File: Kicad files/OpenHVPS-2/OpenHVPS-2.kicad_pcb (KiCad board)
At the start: 2 copper layers, 47.1 x 20.5 mm, 67 parts, among them J1 Conn_01x03_Male, J2 Conn_01x03_Male, Q1 FQT7N10, Q2 BC846, Q3 MMDT3906, U1 74HC14, U2 MAX4162, U3 CD14538BM, U4 MAX6008AEUR+T

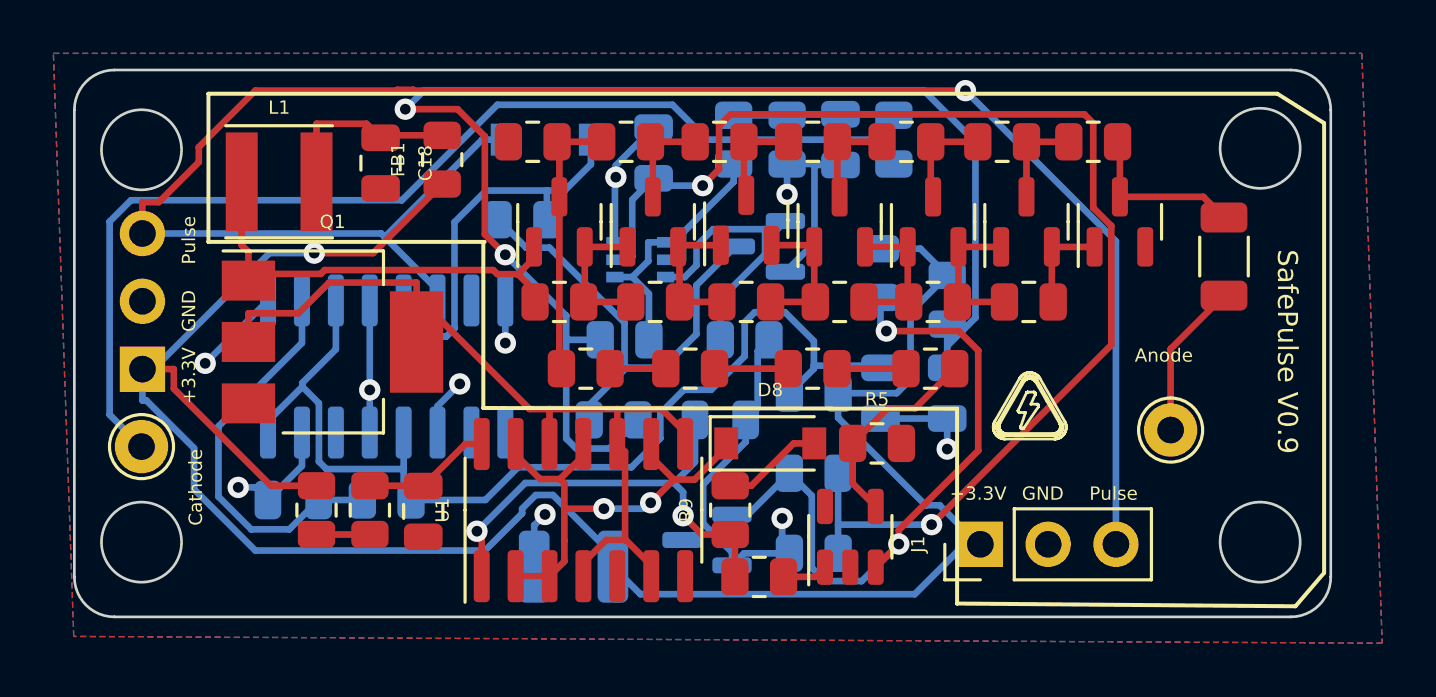
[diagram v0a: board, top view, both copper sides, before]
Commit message: Moved components around and routed again.
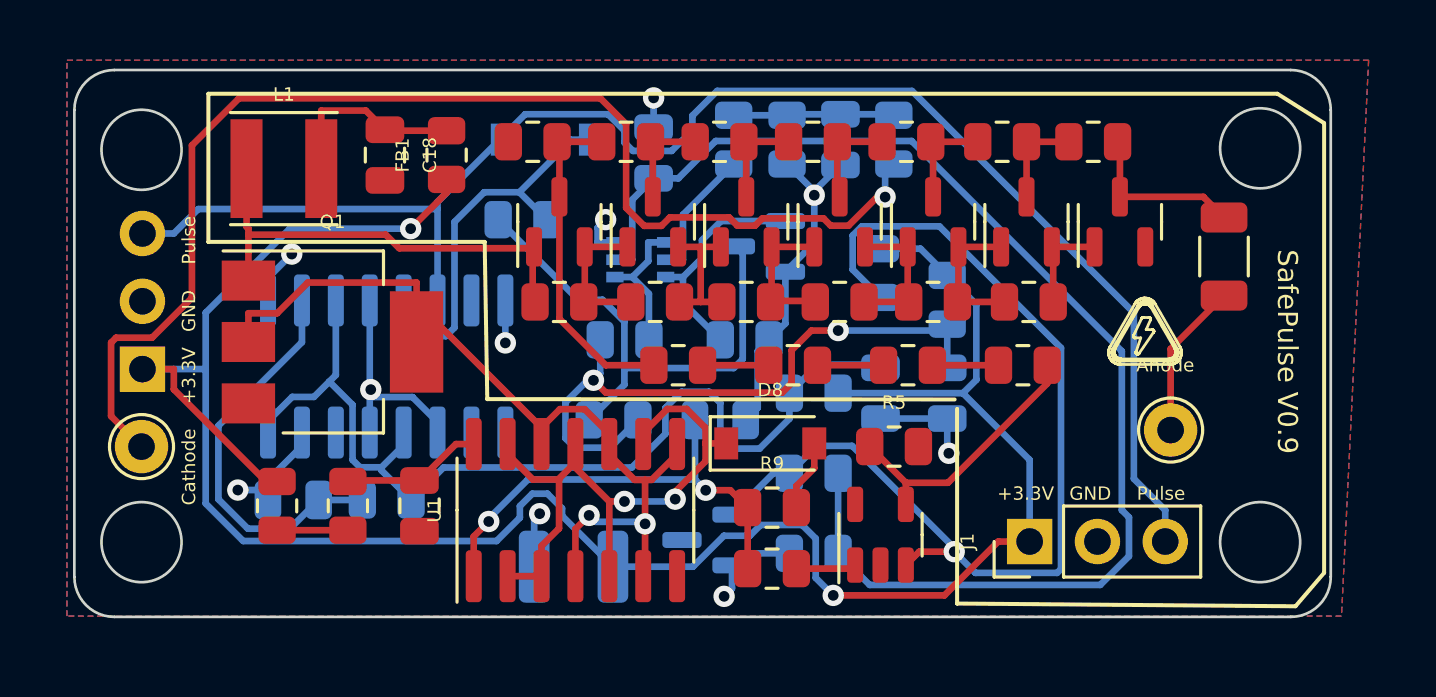
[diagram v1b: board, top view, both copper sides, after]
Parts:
- moved R2 3.86 mm to (147.9, 68.1)
- moved R3 3.57 mm to (152.2, 68.1)
- moved R1 3.47 mm to (143.6, 68.1)
- moved R4 3.47 mm to (156.5, 68.1)
- moved J1 1.85 mm to (156.7, 74.7)
- moved R9 1.57 mm to (147.1, 73.4), turned to 0 degrees
- moved FB2 1.48 mm to (128.5, 73.3)
- moved U2 1.13 mm to (151.1, 74.4)
- moved R10 0.84 mm to (131.2, 73.3)
- moved R5 0.65 mm to (151.6, 71.1)
- moved R8 0.57 mm to (147.1, 75.7)
- moved L1 0.53 mm to (128.8, 60.7)
- moved C18 0.34 mm to (132.6, 60.2)
- moved U1 0.30 mm to (139.7, 73.5)
- moved C15 0.25 mm to (133.9, 73.3)
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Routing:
- net Net-(C21-Pad1): track 52.7 -> 24.4 mm
- net Net-(D9-Pad2): track 71.7 -> 57.3 mm, vias 1 -> 0
- net +2V5: track 25.5 -> 38.4 mm, vias 2 -> 1
- net GND: track 48.4 -> 40.8 mm
- net Net-(D8-Pad1): track 18.2 -> 24.0 mm
- net Net-(H2-Pad1): track 41.0 -> 46.6 mm, vias 0 -> 1
- net +3V3: track 80.8 -> 84.6 mm, vias 1 -> 2
- net Net-(R4-Pad1): track 7.70 -> 10.2 mm
- net Net-(C1-Pad2): track 10.2 -> 12.6 mm
- net Net-(C19-Pad1): track 39.6 -> 37.7 mm
- net Net-(Q2-Pad1): track 10.6 -> 8.68 mm
- net Net-(Q2-Pad3): track 17.6 -> 19.4 mm
- net Net-(D8-Pad2): track 3.81 -> 2.68 mm
- net Net-(C20-Pad1): track 47.4 -> 48.0 mm, vias 2 -> 0
- net Net-(FB2-Pad2): track 2.00 -> 2.65 mm
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
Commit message: small changes board layout and rerouted
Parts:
- moved R7 5.20 mm to (160.3, 67.6)
- moved H5 3.81 mm to (164.1, 67.3)
- moved J1 1.95 mm to (154.8, 75.2)
- moved Q1 0.45 mm to (130.8, 66.8)
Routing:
- net Net-(Q2-Pad3): track 19.4 -> 50.1 mm, vias 0 -> 2
- net +3V3: track 84.6 -> 96.1 mm, vias 2 -> 0
- net Net-(D9-Pad2): track 57.3 -> 67.2 mm
- net +2V5: track 38.4 -> 31.0 mm, vias 1 -> 2
- net GND: track 40.8 -> 46.7 mm
- net Net-(C21-Pad1): track 24.4 -> 18.9 mm, vias 2 -> 0
- net Net-(C19-Pad1): track 37.7 -> 32.5 mm
- net Net-(H2-Pad1): track 46.6 -> 42.7 mm, vias 1 -> 0
- net Net-(Q1-Pad2): track 33.4 -> 30.2 mm, vias 2 -> 0
- net Net-(C2-Pad1): track 17.2 -> 20.1 mm
- net Net-(H5-Pad1): track 5.87 -> 4.55 mm
- net Net-(C16-Pad1): track 15.0 -> 14.1 mm
- net Net-(Q2-Pad1): track 8.68 -> 7.87 mm
- net Net-(D8-Pad1): track 24.0 -> 23.8 mm, vias 2 -> 3
- net Net-(C20-Pad1): track 48.0 -> 48.1 mm, vias 0 -> 2
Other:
- board size 47.1 x 20.5 mm -> 45.4 x 20.1 mm
